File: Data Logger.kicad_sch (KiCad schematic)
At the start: 25 parts, among them U1 24LC1025, U2 DS1339U-3+, U3 24LC1025, U4 ATMEGA328P-AU, Y1 32.768 KHz, Y2 16 MHz

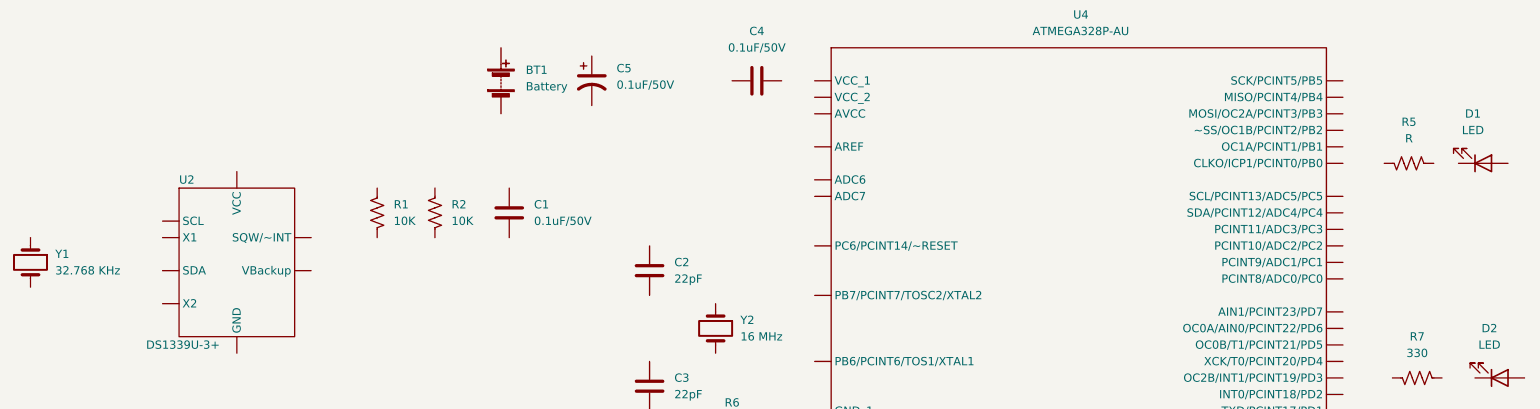
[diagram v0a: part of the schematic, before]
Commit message: Completed Symbol to footprint associations
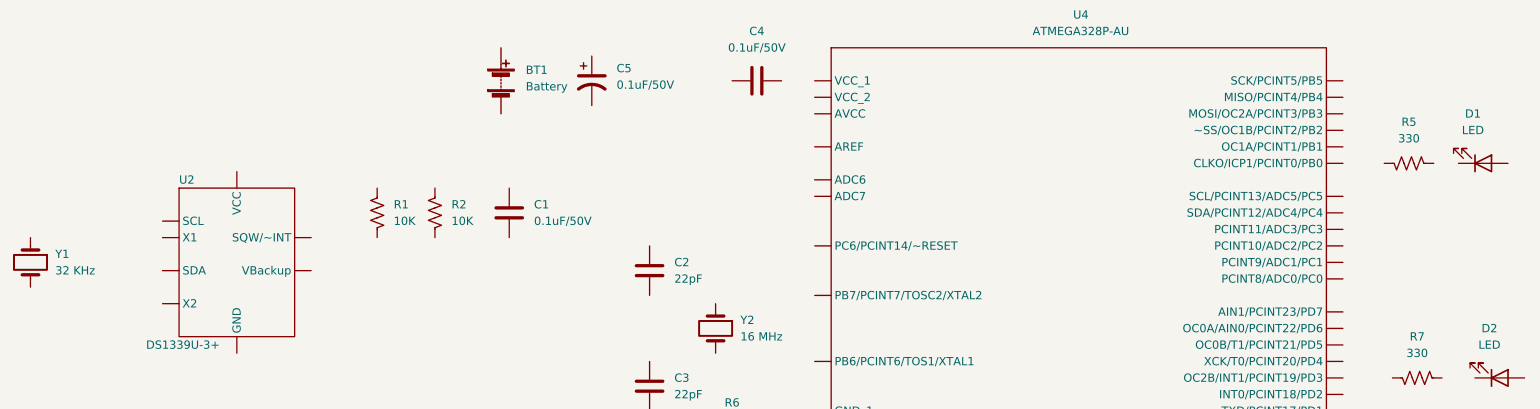
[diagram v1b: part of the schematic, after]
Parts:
- BT1: footprint (none) -> RN_Connectors:J_PTH_CONN_HEADER_MALE_01x02_WUE_61300211121
- C1, C4: footprint (none) -> RN_Capacitors:C_SMD_0.1UF50V_0805_TDK_C2012X8R1H104K125AA
- C2, C3: footprint (none) -> RN_Capacitors:C_SMD_22PF50V_0603_TDK_CGA3E2NP01H220J080AA
- C5: footprint (none) -> RN_Capacitors:C_POL_SMD_0.1UF50V_WUE_865230640001
- D1, D2: footprint (none) -> RN_LED:D_SMD_LED_GREEN_0805_WUE_150080GS75000
- H1, H2, H3, H4: footprint (none) -> RN_Mounting:MOUNTINGHOLE_2.1MM
- R1, R2, R6: footprint (none) -> RN_Resistors:R_SMD_10K_0805_YAG_RC0805FR-0710KL
- R3, R4: footprint (none) -> RN_Resistors:R_SMD_4.7K_0805_YAG_RC0805FR-071KL
- R5: value R -> 330; footprint (none) -> RN_Resistors:R_SMD_330R_0805_YAG_RC0805FR-07330RL
- R7: footprint (none) -> RN_Resistors:R_SMD_330R_0805_YAG_RC0805FR-07330RL
- U1, U3: footprint (none) -> RN_IC_Memory:U_SMD_24LC1025_SOIC-08_MIC_24LC1025T-ESN
- U2: footprint (none) -> RN_IC_RTC:U_SMD_DS1339U_DIP08_ANA_DS1339U-3+
- U4: footprint (none) -> RN_IC_Microcontrollers:U_SMD_ATMEGA320P-AU_QFP-32_MIC_ATMEGA328P-AU
- Y1: value 32.768 KHz -> 32 KHz; footprint (none) -> RN_Crystals:Y_SMD_CRYSTAL_32K_L5.0MMXW3.20_ABR_ABM3-32.000MHZ-D2Y-T
- Y2: footprint (none) -> RN_Crystals:Y_SMD_CRYSTAL_16K_L5.0MMXW3.20_ABR_ABM3-16.000MHZ-B2-T

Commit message: update schematics
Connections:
- net GND: now reaches D2.1 (K)
- net GND: now also BT1.2 (-), C1.2, C2.2, C3.1, C4.2, C5.2, D1.1 (K), U1.4 (GND), U1.7 (WP), U2.4 (GND), U3.2 (A1), U3.4 (GND), U3.7 (WP), U4.21 (GND_3), U4.3 (GND_1), U4.5 (GND_2)
- net at D2.2 (A): now also R7.1
- net Vcc: now reaches R3.1
- net Vcc: now also C1.1, R1.2, R2.2, R4.1, R6.2, U1.1 (A0), U1.2 (A1), U1.3 (A2), U1.8 (VCC), U2.8 (VCC), U3.1 (A0), U3.3 (A2), U3.8 (VCC)
- net SCK: now reaches R3.2
- net SCK: now also R7.2, U1.6 (SCL), U2.6 (SCL), U3.6 (SCL), U4.17 (SCK/PCINT5/PB5), U4.28 (SCL/PCINT13/ADC5/PC5)
- net SDA: now reaches U1.5 (SDA)
- net SDA: now also R4.2, U2.5 (SDA), U3.5 (SDA), U4.27 (SDA/PCINT12/ADC4/PC4)
- net at C5.1: now also BT1.1 (+), R5.2, U4.18 (AVCC), U4.4 (VCC_1)
- net RESET: now reaches R6.1
- net RESET: now also U4.29 (PC6/PCINT14/~RESET)
- net at Y2.1: now also C2.1, U4.7 (PB6/PCINT6/TOS1/XTAL1)
- net at Y2.2: now also C3.2, U4.8 (PB7/PCINT7/TOSC2/XTAL2)
- net at Y1.1: now also U2.1 (X1)
- net at Y1.2: now also U2.2 (X2)
- net at R1.1: now also U2.3 (VBackup)
- net at C4.1: now also U4.20 (AREF)
- net at R2.1: now also U2.7 (SQW/~INT)
- net at R5.1: now also D1.2 (A)
- new net D2: U4.32 (INT0/PCINT18/PD2)
- new net D3: U4.1 (OC2B/INT1/PCINT19/PD3)
- new net D4: U4.2 (XCK/T0/PCINT20/PD4)
- new net D5: U4.9 (OC0B/T1/PCINT21/PD5)
- new net D6: U4.10 (OC0A/AIN0/PCINT22/PD6)
- new net D7: U4.11 (AIN1/PCINT23/PD7)
- new net D8: U4.12 (CLKO/ICP1/PCINT0/PB0)
- new net MISO: U4.16 (MISO/PCINT4/PB4)
- new net MOSI: U4.15 (MOSI/OC2A/PCINT3/PB3)
- new net RX: U4.30 (RXD/PCINT16/PD0)
- new net TX: U4.31 (TXD/PCINT17/PD1)
- no-connect marks 0 -> 9
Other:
- sheet Connectors ports: added D2, D3, D4, D5, D6, D7, D8, GND, MISO, MOSI, RESET, RX, SCK, SDA, TX, Vcc; removed none
- moved on the sheet: BT1, C1, C2, C3, C4, C5, D1, D2, H1, H2, H3, H4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

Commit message: Completed Routing
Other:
- moved on the sheet: BT1, C2, C3, C5, H1, H2, H3, H4, Y2

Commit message: Fixed Routing
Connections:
- net Vcc: now also BT1.1 (+), C5.1, R5.2, U4.18 (AVCC), U4.4 (VCC_1)
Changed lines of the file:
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@@
+    (effects (font (size 1.27 1.27)) (justify left bottom))
+  )
+  (label "Vcc" (at 102.87 30.48 0)
     (effects (font (size 1.27 1.27)) (justify left bottom))
   )

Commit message: routing
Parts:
- U2: footprint RN_IC_RTC:U_SMD_DS1339U_DIP08_ANA_DS1339U-3+ -> RN_IC_RTC:U_SMD_DS1339U_TSSOP08_ANA_DS1339U-3+
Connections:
- net GND: now also R7.1; no longer D2.1 (K)
- net SCK: now also D2.2 (A); no longer R7.2
- new net: D2.1 (K), R7.2
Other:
- moved on the sheet: D2, R7
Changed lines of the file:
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@@
+    (stroke (width 0) (type default) (color 0 0 0 0))
+  )
+  (wire (pts (xy 237.49 25.4) (xy 241.3 25.4))
     (stroke (width 0) (type default) (color 0 0 0 0))
   )
@@
     (stroke (width 0) (type default) (color 0 0 0 0))
   )
+  (wire (pts (xy 248.92 25.4) (xy 251.46 25.4))
+    (stroke (width 0) (type default) (color 0 0 0 0))
+  )
   (wire (pts (xy 95.25 168.91) (xy 95.25 166.37))
     (stroke (width 0) (type default) (color 0 0 0 0))
   )
-  (wire (pts (xy 220.98 25.4) (xy 227.33 25.4))
-    (stroke (width 0) (type default) (color 0 0 0 0))
-  )
   (wire (pts (xy 43.18 170.18) (xy 45.72 170.18))
     (stroke (width 0) (type default) (color 0 0 0 0))
@@
     (stroke (width 0) (type default) (color 0 0 0 0))
   )
-  (wire (pts (xy 251.46 25.4) (xy 246.38 25.4))
-    (stroke (width 0) (type default) (color 0 0 0 0))
-  )
   (wire (pts (xy 36.83 128.27) (xy 40.64 128.27))
     (stroke (width 0) (type default) (color 0 0 0 0))
@@
     (stroke (width 0) (type default) (color 0 0 0 0))
   )
+  (wire (pts (xy 220.98 25.4) (xy 229.87 25.4))
+    (stroke (width 0) (type default) (color 0 0 0 0))
+  )
   (wire (pts (xy 110.49 30.48) (xy 97.79 30.48))
     (stroke (width 0) (type default) (color 0 0 0 0))
@@
     (stroke (width 0) (type default) (color 0 0 0 0))
   )
-  (wire (pts (xy 234.95 25.4) (xy 238.76 25.4))
-    (stroke (width 0) (type default) (color 0 0 0 0))
-  )
   (wire (pts (xy 97.79 30.48) (xy 97.79 31.75))
     (stroke (width 0) (type default) (color 0 0 0 0))
@@
     (effects (font (size 1.27 1.27)) (justify left bottom))
   )
+  (label "TX" (at 209.55 129.54 0)
+    (effects (font (size 1.27 1.27)) (justify left bottom))
+  )
+  (label "D7" (at 223.52 60.96 0)
+    (effects (font (size 1.27 1.27)) (justify left bottom))
+  )
+  (label "D6" (at 223.52 63.5 0)
+    (effects (font (size 1.27 1.27)) (justify left bottom))
+  )
+  (label "SDA" (at 223.52 45.72 0)
+    (effects (font (size 1.27 1.27)) (justify left bottom))
+  )
+  (label "SCK" (at 209.55 120.65 0)
+    (effects (font (size 1.27 1.27)) (justify left bottom))
+  )
+  (label "D7" (at 260.35 130.81 0)
+    (effects (font (size 1.27 1.27)) (justify left bottom))
+  )
+  (label "Vcc" (at 99.06 163.83 0)
+    (effects (font (size 1.27 1.27)) (justify left bottom))
+  )
+  (label "SCK" (at 223.52 43.18 0)
+    (effects (font (size 1.27 1.27)) (justify left bottom))
+  )
+  (label "SDA" (at 209.55 118.11 0)
+    (effects (font (size 1.27 1.27)) (justify left bottom))
+  )
+  (label "D4" (at 223.52 68.58 0)
+    (effects (font (size 1.27 1.27)) (justify left bottom))
+  )
+  (label "D5" (at 260.35 125.73 0)
+    (effects (font (size 1.27 1.27)) (justify left bottom))
+  )
+  (label "Vcc" (at 57.15 170.18 0)
+    (effects (font (size 1.27 1.27)) (justify left bottom))
+  )
+  (label "RX" (at 209.55 132.08 0)
+    (effects (font (size 1.27 1.27)) (justify left bottom))
+  )
+  (label "SDA" (at 104.14 179.07 0)
+    (effects (font (size 1.27 1.27)) (justify left bottom))
+  )
+  (label "D8" (at 223.52 38.1 0)
+    (effects (font (size 1.27 1.27)) (justify left bottom))
+  )
+  (label "Vcc" (at 143.51 46.99 0)
+    (effects (font (size 1.27 1.27)) (justify left bottom))
+  )
+  (label "Vcc" (at 33.02 162.56 0)
+    (effects (font (size 1.27 1.27)) (justify left bottom))
+  )
   (label "SCK" (at 223.52 25.4 0)
     (effects (font (size 1.27 1.27)) (justify left bottom))
   )
-  (label "TX" (at 209.55 129.54 0)
-    (effects (font (size 1.27 1.27)) (justify left bottom))
-  )
-  (label "D7" (at 223.52 60.96 0)
-    (effects (font (size 1.27 1.27)) (justify left bottom))
-  )
-  (label "D6" (at 223.52 63.5 0)
-    (effects (font (size 1.27 1.27)) (justify left bottom))
-  )
-  (label "SDA" (at 223.52 45.72 0)
-    (effects (font (size 1.27 1.27)) (justify left bottom))
-  )
-  (label "SCK" (at 209.55 120.65 0)
-    (effects (font (size 1.27 1.27)) (justify left bottom))
-  )
-  (label "D7" (at 260.35 130.81 0)
-    (effects (font (size 1.27 1.27)) (justify left bottom))
-  )
-  (label "Vcc" (at 99.06 163.83 0)
-    (effects (font (size 1.27 1.27)) (justify left bottom))
-  )
-  (label "SCK" (at 223.52 43.18 0)
-    (effects (font (size 1.27 1.27)) (justify left bottom))
-  )
-  (label "SDA" (at 209.55 118.11 0)
-    (effects (font (size 1.27 1.27)) (justify left bottom))
-  )
-  (label "D4" (at 223.52 68.58 0)
-    (effects (font (size 1.27 1.27)) (justify left bottom))
-  )
-  (label "D5" (at 260.35 125.73 0)
-    (effects (font (size 1.27 1.27)) (justify left bottom))
-  )
-  (label "Vcc" (at 57.15 170.18 0)
-    (effects (font (size 1.27 1.27)) (justify left bottom))
-  )
-  (label "RX" (at 209.55 132.08 0)
-    (effects (font (size 1.27 1.27)) (justify left bottom))
-  )
-  (label "SDA" (at 104.14 179.07 0)
-    (effects (font (size 1.27 1.27)) (justify left bottom))
-  )
-  (label "D8" (at 223.52 38.1 0)
-    (effects (font (size 1.27 1.27)) (justify left bottom))
-  )
-  (label "Vcc" (at 143.51 46.99 0)
-    (effects (font (size 1.27 1.27)) (justify left bottom))
-  )
-  (label "Vcc" (at 33.02 162.56 0)
-    (effects (font (size 1.27 1.27)) (justify left bottom))
-  )
   (label "D3" (at 223.52 71.12 0)
     (effects (font (size 1.27 1.27)) (justify left bottom))
@@
     (effects (font (size 1.27 1.27)) (justify left bottom))
   )
-  (symbol (lib_id "RN_LED:LED") (at 243.84 25.4 0) (unit 1)
-    (in_bom yes) (on_board yes) (fields_autoplaced)
-    (property "Reference" "D2" (id 0) (at 244.1575 19.05 0))
-    (property "Value" "LED" (id 1) (at 244.1575 21.59 0))
-    (property "Footprint" "RN_LED:D_SMD_LED_GREEN_0805_WUE_150080GS75000" (id 2) (at 242.57 31.75 0)
-      (effects (font (size 1.27 1.27)) hide)
-    )
-    (property "Datasheet" "~" (id 3) (at 242.57 25.4 0)
+  (symbol (lib_id "RN_LED:LED") (at 234.95 25.4 0) (unit 1)
+    (in_bom yes) (on_board yes) (fields_autoplaced)
+    (property "Reference" "D2" (id 0) (at 235.2675 19.05 0))
+    (property "Value" "LED" (id 1) (at 235.2675 21.59 0))
+    (property "Footprint" "RN_LED:D_SMD_LED_GREEN_0805_WUE_150080GS75000" (id 2) (at 233.68 31.75 0)
+      (effects (font (size 1.27 1.27)) hide)
+    )
+    (property "Datasheet" "~" (id 3) (at 233.68 25.4 0)
       (effects (font (size 1.27 1.27)) hide)
     )
@@
       (effects (font (size 1.27 1.27)) (justify left))
     )
-    (property "Footprint" "RN_IC_RTC:U_SMD_DS1339U_DIP08_ANA_DS1339U-3+" (id 2) (at 53.34 110.49 0)
+    (property "Footprint" "RN_IC_RTC:U_SMD_DS1339U_TSSOP08_ANA_DS1339U-3+" (id 2) (at 53.34 110.49 0)
       (effects (font (size 1.27 1.27)) hide)
     )
@@
     (pin "1")
   )
-  (symbol (lib_id "RN_Resistors:R") (at 231.14 25.4 0) (unit 1)
-    (in_bom yes) (on_board yes) (fields_autoplaced)
-    (property "Reference" "R7" (id 0) (at 231.14 19.05 0))
-    (property "Value" "330" (id 1) (at 231.14 21.59 0))
-    (property "Footprint" "RN_Resistors:R_SMD_330R_0805_YAG_RC0805FR-07330RL" (id 2) (at 232.41 30.48 0)
-      (effects (font (size 1.27 1.27)) hide)
-    )
-    (property "Datasheet" "~" (id 3) (at 231.14 25.4 90)
+  (symbol (lib_id "RN_Resistors:R") (at 245.11 25.4 0) (unit 1)
+    (in_bom yes) (on_board yes) (fields_autoplaced)
+    (property "Reference" "R7" (id 0) (at 245.11 19.05 0))
+    (property "Value" "330" (id 1) (at 245.11 21.59 0))
+    (property "Footprint" "RN_Resistors:R_SMD_330R_0805_YAG_RC0805FR-07330RL" (id 2) (at 246.38 30.48 0)
+      (effects (font (size 1.27 1.27)) hide)
+    )
+    (property "Datasheet" "~" (id 3) (at 245.11 25.4 90)
       (effects (font (size 1.27 1.27)) hide)
     )
@@
     )
     (path "/6ad39032-1336-48b5-88bc-beea22c50f9e"
-      (reference "U2") (unit 1) (value "DS1339U-3+") (footprint "RN_IC_RTC:U_SMD_DS1339U_DIP08_ANA_DS1339U-3+")
+      (reference "U2") (unit 1) (value "DS1339U-3+") (footprint "RN_IC_RTC:U_SMD_DS1339U_TSSOP08_ANA_DS1339U-3+")
     )
     (path "/9196be21-daf1-4f74-a620-716eee54d8d8"
